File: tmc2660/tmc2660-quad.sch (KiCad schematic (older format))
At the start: 15 parts, among them P3 Motor, U1 TMC2660

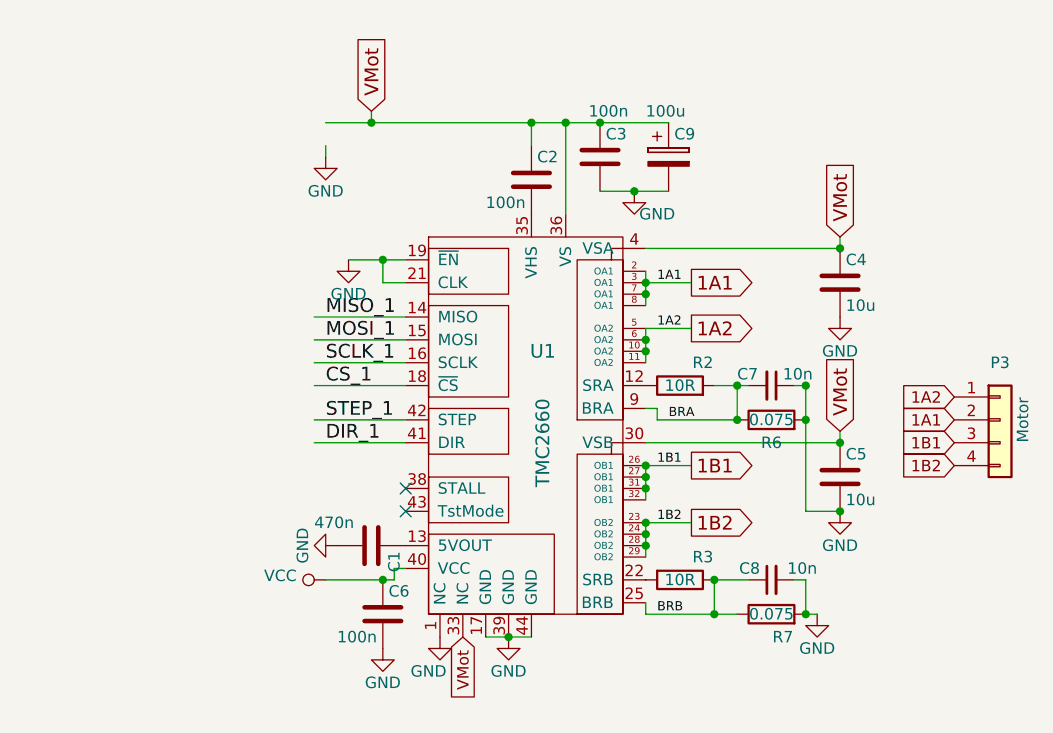
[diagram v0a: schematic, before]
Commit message: Wire up SPI in signal layer; prepare Step/Dir.
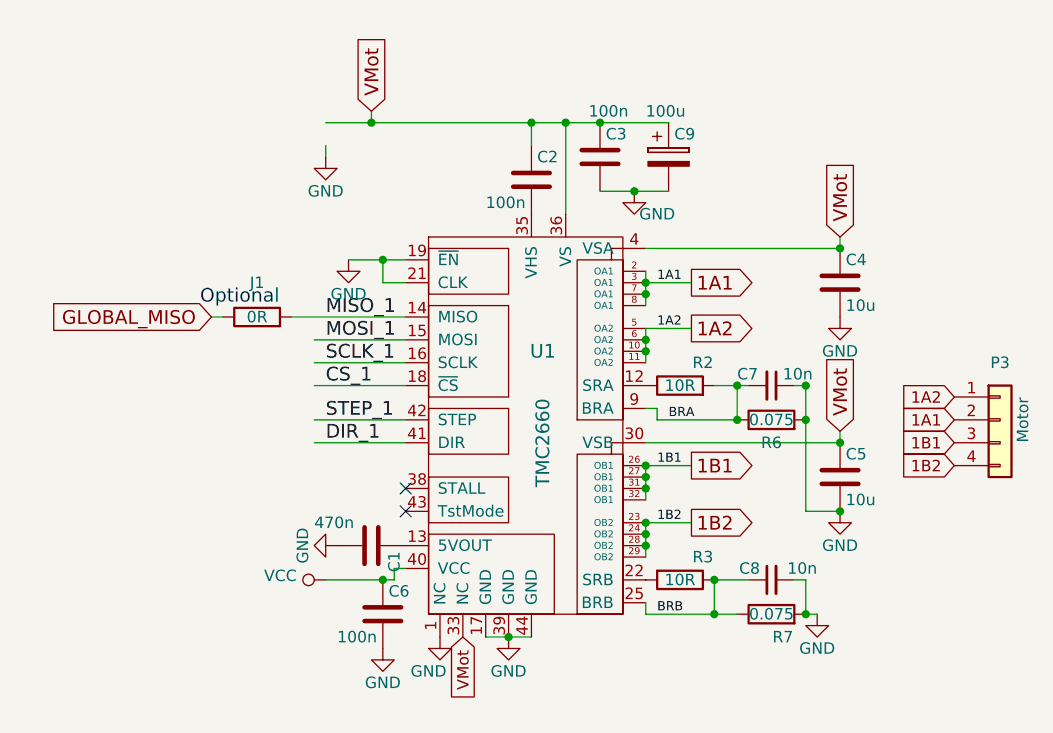
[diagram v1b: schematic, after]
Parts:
- added J1: 0R, Resistors_SMD:R_0603, symbol R
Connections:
- net labels added: GLOBAL_MISO
- wire segments 48 -> 49
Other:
- note added: "Optional"
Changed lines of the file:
@@
 LIBS:tmc2660
 LIBS:Connector
-LIBS:tmc2660-quadrigotion-cache
+LIBS:tmc2660-quad-cache
 EELAYER 26 0
 EELAYER END
@@
 	2900 3950 2850 3950
 Wire Wire Line
-	2850 3950 2850 4000
-Wire Wire Line
-	2850 4000 2550 4000
+	2850 4000 2850 3950
+Wire Wire Line
+	2550 4000 2850 4000
 Text GLabel 3150 4250 3    50   Input ~ 0
 VMot
@@
 $EndComp
 Wire Wire Line
-	2900 2850 2500 2850
+	2900 2850 2400 2850
 Wire Wire Line
 	2900 2950 2500 2950
@@
 	3750 2300 4050 2300
 Connection ~ 3900 2300
+Text GLabel 2050 2850 0    60   Input ~ 0
+GLOBAL_MISO
+$Comp
+L R J1
+U 1 1 5A0A53B6
+P 2250 2850
+F 0 "J1" V 2400 2850 50  0000 C CNN
+F 1 "0R" V 2250 2850 50  0000 C CNN
+F 2 "Resistors_SMD:R_0603" V 2180 2850 30  0001 C CNN
+F 3 "" H 2250 2850 30  0000 C CNN
+	1    2250 2850
+	0    -1   -1   0
+$EndComp
+Wire Wire Line
+	2050 2850 2100 2850
+Text Notes 2000 2800 0    60   ~ 0
+Optional
 $EndSCHEMATC
